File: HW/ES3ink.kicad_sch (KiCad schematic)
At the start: 72 parts, among them J1 USB_C_Receptacle_USB2.0, J2 Conn_01x24_Pin, J2 USB_C_Receptacle_USB2.0, J3 Conn_01x02_Pin, J4 Conn_01x04_Socket, Q1 DMG3415U-7, Q2 SI1308EDL-T1-GE3, Q3 DMG3415U-7, Q4 SI2305, SW1 RESET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

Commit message: Version 2.5 upload
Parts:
- removed T1, T2, T3, T4: Tab, PCM_kikit:Tab, symbol PCM_kikit:Tab
- added JP3: SolderJumper_2_Open, Jumper:SolderJumper-2_P1.3mm_Open_TrianglePad1.0x1.5mm, symbol Jumper:SolderJumper_2_Open
- L1: value 68uH -> 10uH/1A
- R10: value 10R -> 2R2
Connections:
- net 3V3_EPD: now also Q1.3 (D); no longer R10.2
- net GND: now also R10.2, JP3.2 (B); no longer R9.2
- net at R10.1: now also R9.2, JP3.1 (A); no longer Q1.3 (D)
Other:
- note added: "Pin connection: EN : Reset button IO0 : Boot button IO1 : IO2 : Battery reading IO3 : Qwiic SCL IO4 : Qwiic SDA IO5 : EPD Reset IO6 : EPD Busy IO7 : IO8 : RGB LED power IO9 : EPD CS IO10: EPD DC IO11: MOSI IO12: CLK IO13: MISO IO14: IO15: IO16: IO17: IO18: RGB LED data IO19: IO20: USB D+ IO21: USB D- IO38: Double Reset IO39: IO40: Enable battery reading IO41: IO42: IO43: IO44: IO45: IO46: IO47: I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"
- note removed: "Pin connection: EN : Reset button IO0 : Boot button IO1 : IO2 : IO3 : Qwiic SCL IO4 : Qwiic SDA IO5 : EPD Reset IO6 : EPD Busy IO7 : IO8 : IO9 : EPD CS IO10: EPD DC IO11: MOSI IO12: CLK IO13: MISO IO14: IO15: IO16: IO17: IO18: IO19: IO20: USB D+ IO21: USB D- IO38: Double Reset IO39: IO40: Enable battery reading IO41: IO42: Battery reading IO43: IO44: IO45: IO46: IO47: IO48: EPD power enable"
- moved on the sheet: C13, C14, C19, D1, D2, D3, H1, H2, L1, Q1, Q2, R11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

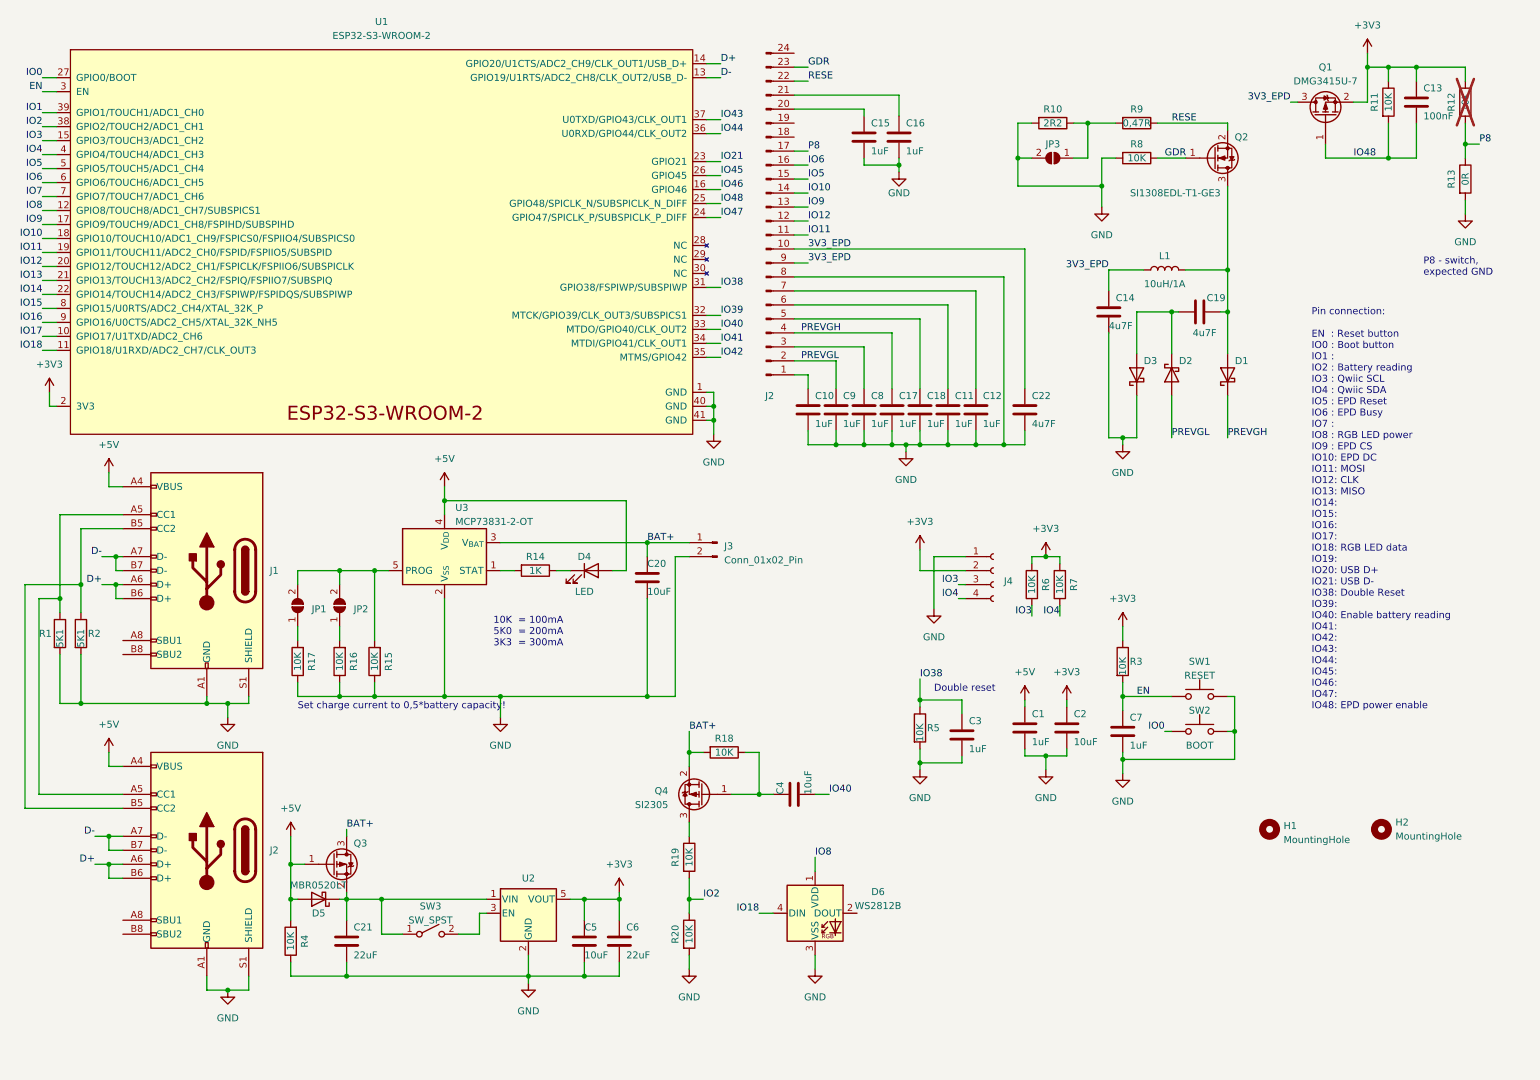
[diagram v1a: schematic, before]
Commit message: Update component values
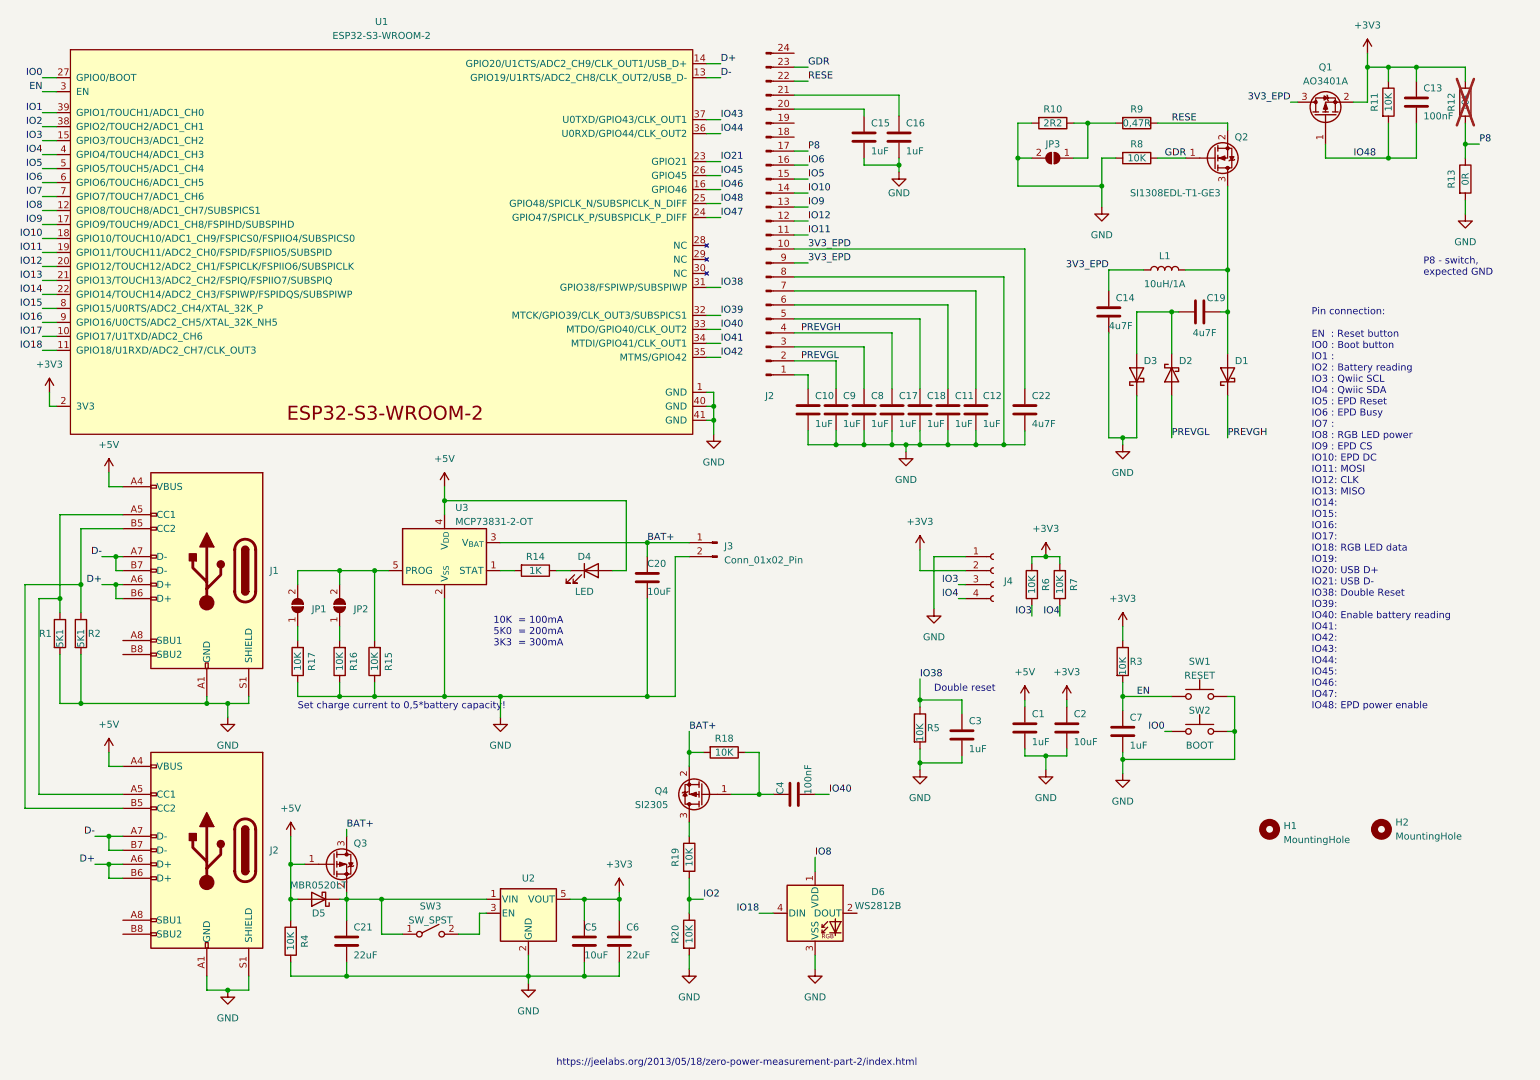
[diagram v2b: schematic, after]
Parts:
- C4: value 10uF -> 100nF
- Q1: value DMG3415U-7 -> AO3401A
- Q3: value DMG3415U-7 -> DMP2045U-7
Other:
- note added: "https://jeelabs.org/2013/05/18/zero-power-measurement-part-2/index.html"
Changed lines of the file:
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@@
     (stroke (width 0) (type default))
+  )
+  (text "https://jeelabs.org/2013/05/18/zero-power-measurement-part-2/index.html"
+    (at 113.03 204.47 0)
+    (effects (font (size 1.27 1.27)) (justify left bottom))
   )
   (text "P8 - switch,\nexpected GND" (at 270.51 60.96 0)
@@
       (effects (font (size 1.27 1.27)))
     )
-    (property "Value" "DMG3415U-7" (at 252.73 25.4 90)
+    (property "Value" "AO3401A" (at 252.73 25.4 90)
       (effects (font (size 1.27 1.27)))
     )
@@
       (effects (font (size 1.27 1.27)) (justify left))
     )
-    (property "Value" "DMG3415U-7" (at 80.01 163.83 0)
+    (property "Value" "DMP2045U-7" (at 80.01 163.83 0)
       (effects (font (size 1.27 1.27)) (justify left) hide)
     )
@@
       (effects (font (size 1.27 1.27)) (justify left))
     )
-    (property "Value" "10uF" (at 158.75 154.94 0)
-      (effects (font (size 1.27 1.27)) (justify left))
-    )
+    (property "Value" "100nF" (at 158.75 154.94 0)
+      (effects (font (size 1.27 1.27)) (justify left))
+    )

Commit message: Update
- pin change to match ESP32-S3 DevKitC 1
- revision change to P1.0 (production)
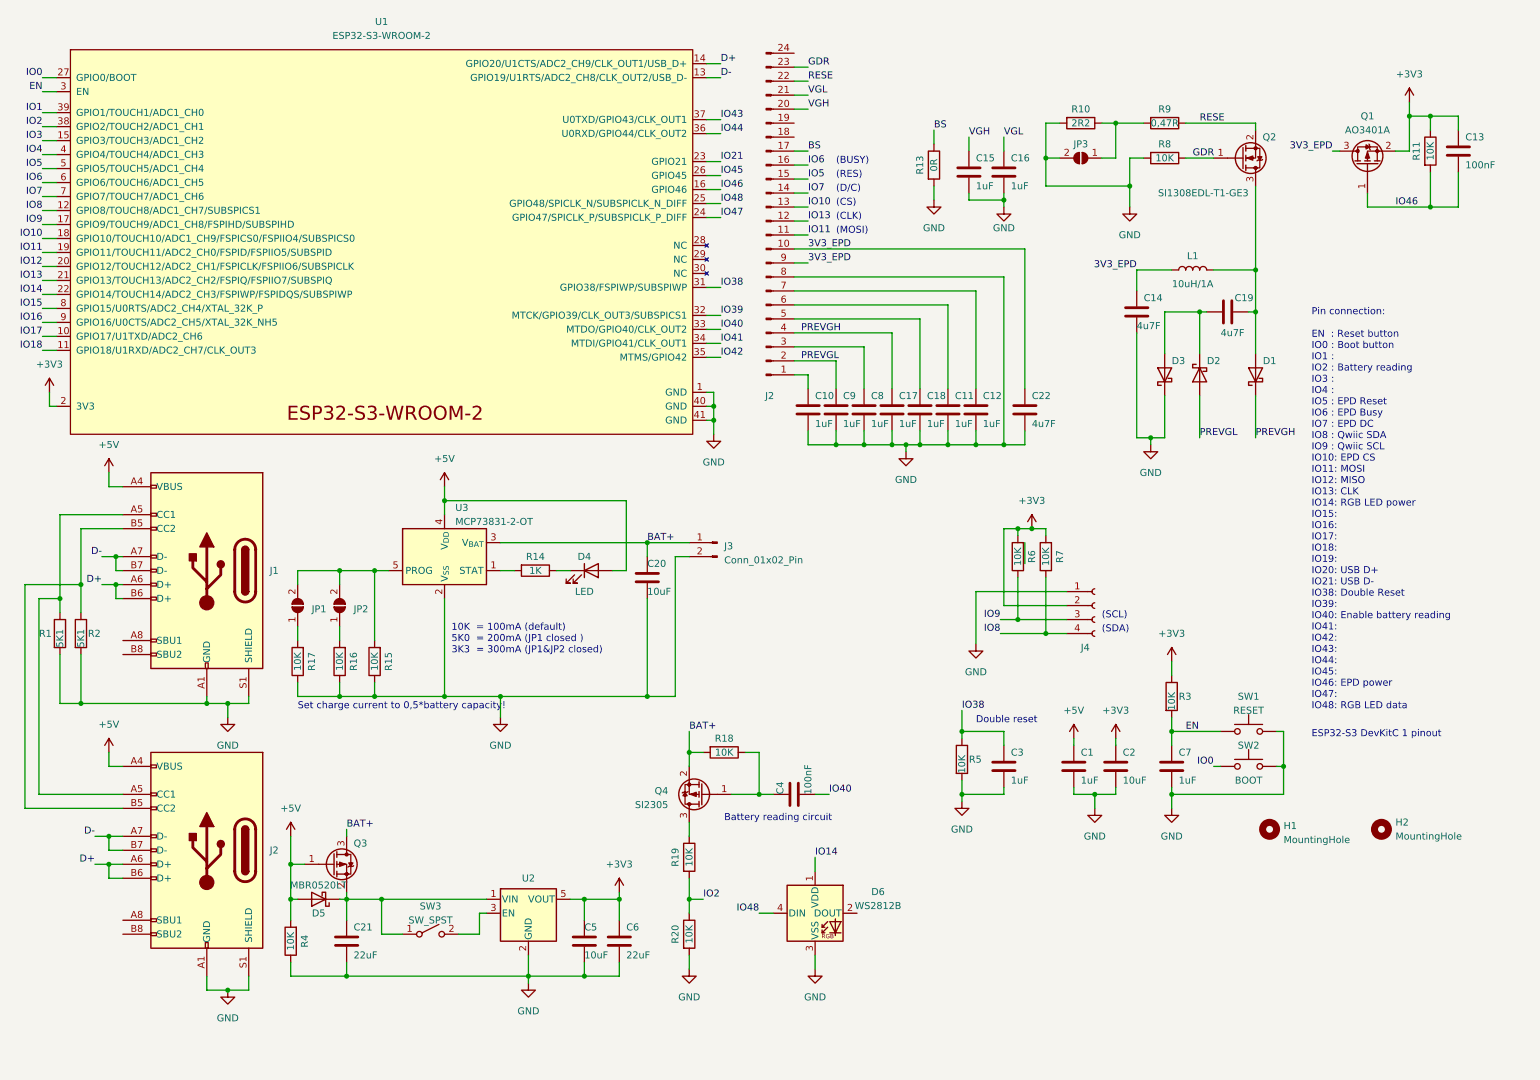
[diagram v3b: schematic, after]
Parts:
- removed R12: 10K, Resistor_SMD:R_0805_2012Metric, symbol Device:R
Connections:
- net IO10: now also J2.13 (Pin_13); no longer J2.14 (Pin_14)
- net IO12: no longer J2.12 (Pin_12)
- net IO13: now also J2.12 (Pin_12)
- net IO14: now also D6.1 (VDD)
- net IO18: no longer D6.4 (DIN)
- net IO3: no longer J4.3 (Pin_3), R6.1
- net IO4: no longer J4.4 (Pin_4), R7.1
- net IO46: now also C13.2, Q1.1 (G), R11.2
- net IO48: now also D6.4 (DIN); no longer C13.2, Q1.1 (G), R11.2
- net IO7: now also J2.14 (Pin_14)
- net IO8: now also J4.4 (Pin_4), R7.1; no longer D6.1 (VDD)
- net IO9: now also J4.3 (Pin_3), R6.1; no longer J2.13 (Pin_13)
- net VGL: now reaches C16.1, J2.21 (Pin_21)
- net VGH: now reaches C15.1, J2.20 (Pin_20)
- net P8 renamed BS
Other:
- note added: "(BUSY)"
- note added: "(CLK)"
- note added: "(CS)"
- note added: "(D/C)"
- note added: "(MOSI)"
- note added: "(RES)"
- note added: "(SCL)"
- note added: "(SDA)"
- note added: "10K = 100mA (default) 5K0 = 200mA (JP1 closed ) 3K3 = 300mA (JP1&JP2 closed)"
- note added: "Battery reading circuit"
- note added: "ESP32-S3 DevKitC 1 pinout"
- note added: "Pin connection: EN : Reset button IO0 : Boot button IO1 : IO2 : Battery reading IO3 : IO4 : IO5 : EPD Reset IO6 : EPD Busy IO7 : EPD DC IO8 : Qwiic SDA IO9 : Qwiic SCL IO10: EPD CS IO11: MOSI IO12: MISO IO13: CLK IO14: RGB LED power IO15: IO16: IO17: IO18: IO19: IO20: USB D+ IO21: USB D- IO38: Double Reset IO39: IO40: Enable battery reading IO41: IO42: IO43: IO44: IO45: IO46: EPD power IO47: IO48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"
- note removed: "10K = 100mA 5K0 = 200mA 3K3 = 300mA"
- note removed: "P8 - switch, expected GND"
- note removed: "Pin connection: EN : Reset button IO0 : Boot button IO1 : IO2 : Battery reading IO3 : Qwiic SCL IO4 : Qwiic SDA IO5 : EPD Reset IO6 : EPD Busy IO7 : IO8 : RGB LED power IO9 : EPD CS IO10: EPD DC IO11: MOSI IO12: CLK IO13: MISO IO14: IO15: IO16: IO17: IO18: RGB LED data IO19: IO20: USB D+ IO21: USB D- IO38: Double Reset IO39: IO40: Enable battery reading IO41: IO42: IO43: IO44: IO45: IO46: IO47: I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"
- note removed: "https://jeelabs.org/2013/05/18/zero-power-measurement-part-2/index.html"
- moved on the sheet: C1, C13, C14, C15, C16, C19, C2, C3, C7, D1, D2, D3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

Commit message: R18 value change
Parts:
- R18: value 10K -> 1M
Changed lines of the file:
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@@
       (effects (font (size 1.27 1.27)))
     )
-    (property "Value" "10K" (at 143.51 147.32 90)
+    (property "Value" "1M" (at 143.51 147.32 90)
       (effects (font (size 1.27 1.27)))
     )

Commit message: Update
- fix I2C pin at Qwiic connector
- fix SPI CLK pin for EPD
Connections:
- net IO12: now also J2.12 (Pin_12)
- net IO13: no longer J2.12 (Pin_12)
- net IO8: now also J4.3 (Pin_3), R6.1; no longer J4.4 (Pin_4), R7.1
- net IO9: now also J4.4 (Pin_4), R7.1; no longer J4.3 (Pin_3), R6.1
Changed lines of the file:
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@@
     (effects (font (size 1.27 1.27)) (justify left bottom))
   )
-  (label "IO8" (at 193.675 125.73 180) (fields_autoplaced)
+  (label "IO8" (at 193.675 123.19 180) (fields_autoplaced)
     (effects (font (size 1.27 1.27)) (justify right bottom))
   )
@@
     (effects (font (size 1.27 1.27)) (justify right bottom))
   )
-  (label "IO9" (at 193.675 123.19 180) (fields_autoplaced)
+  (label "IO9" (at 193.675 125.73 180) (fields_autoplaced)
     (effects (font (size 1.27 1.27)) (justify right bottom))
   )
@@
     (effects (font (size 1.27 1.27)) (justify right bottom))
   )
-  (label "IO13" (at 158.75 50.8 0) (fields_autoplaced)
+  (label "IO12" (at 158.75 50.8 0) (fields_autoplaced)
     (effects (font (size 1.27 1.27)) (justify left bottom))
   )
